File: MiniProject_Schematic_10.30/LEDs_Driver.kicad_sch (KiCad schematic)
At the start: 24 parts, among them U8 IS31FL3254-QFLS4-TR

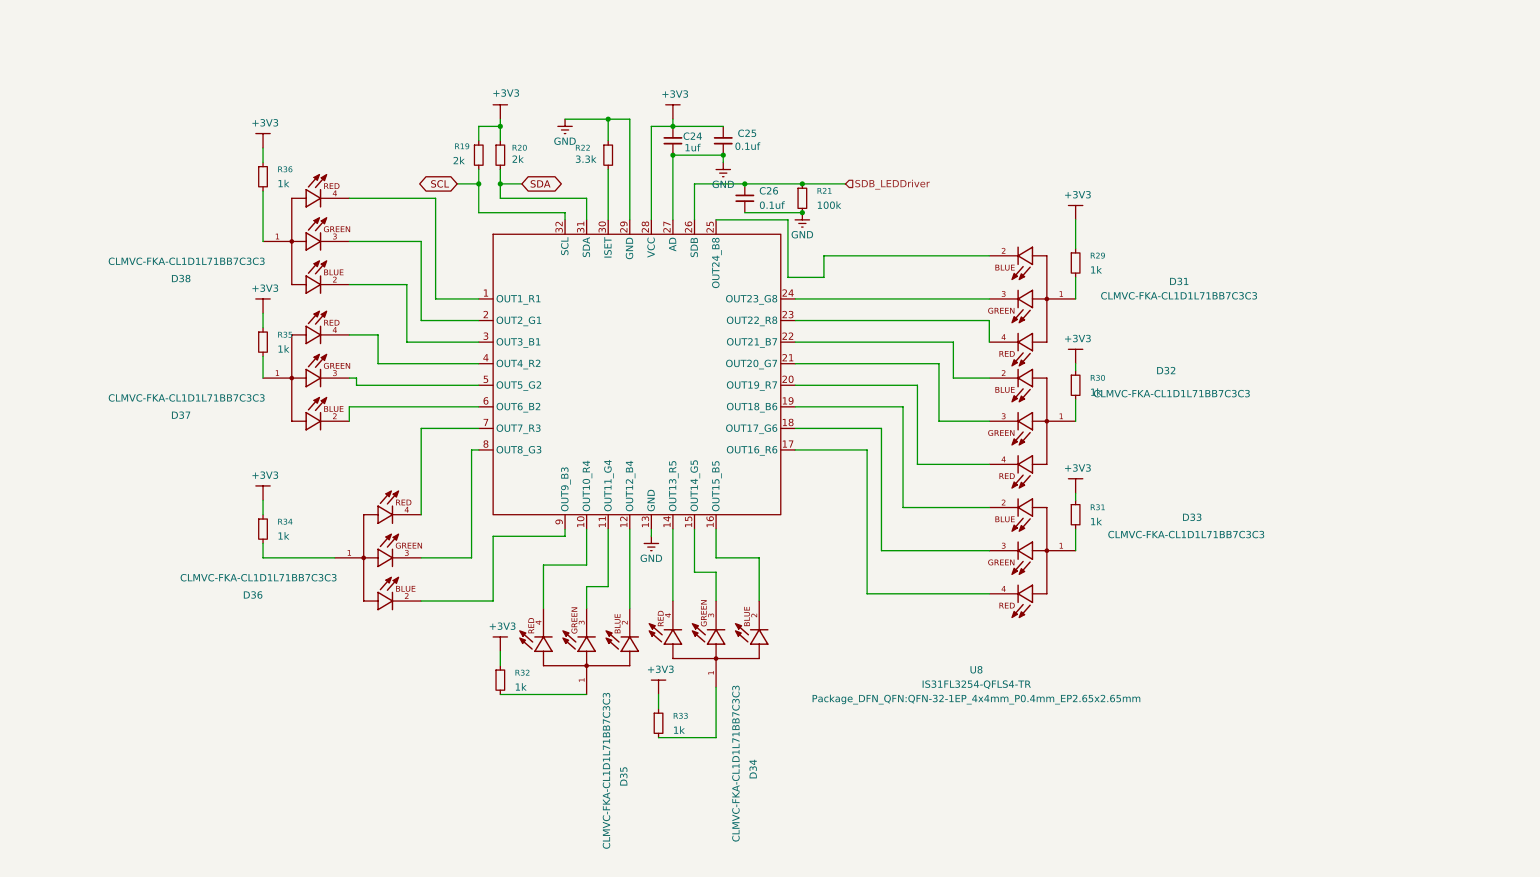
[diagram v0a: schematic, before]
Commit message: Correct the schematic diagram
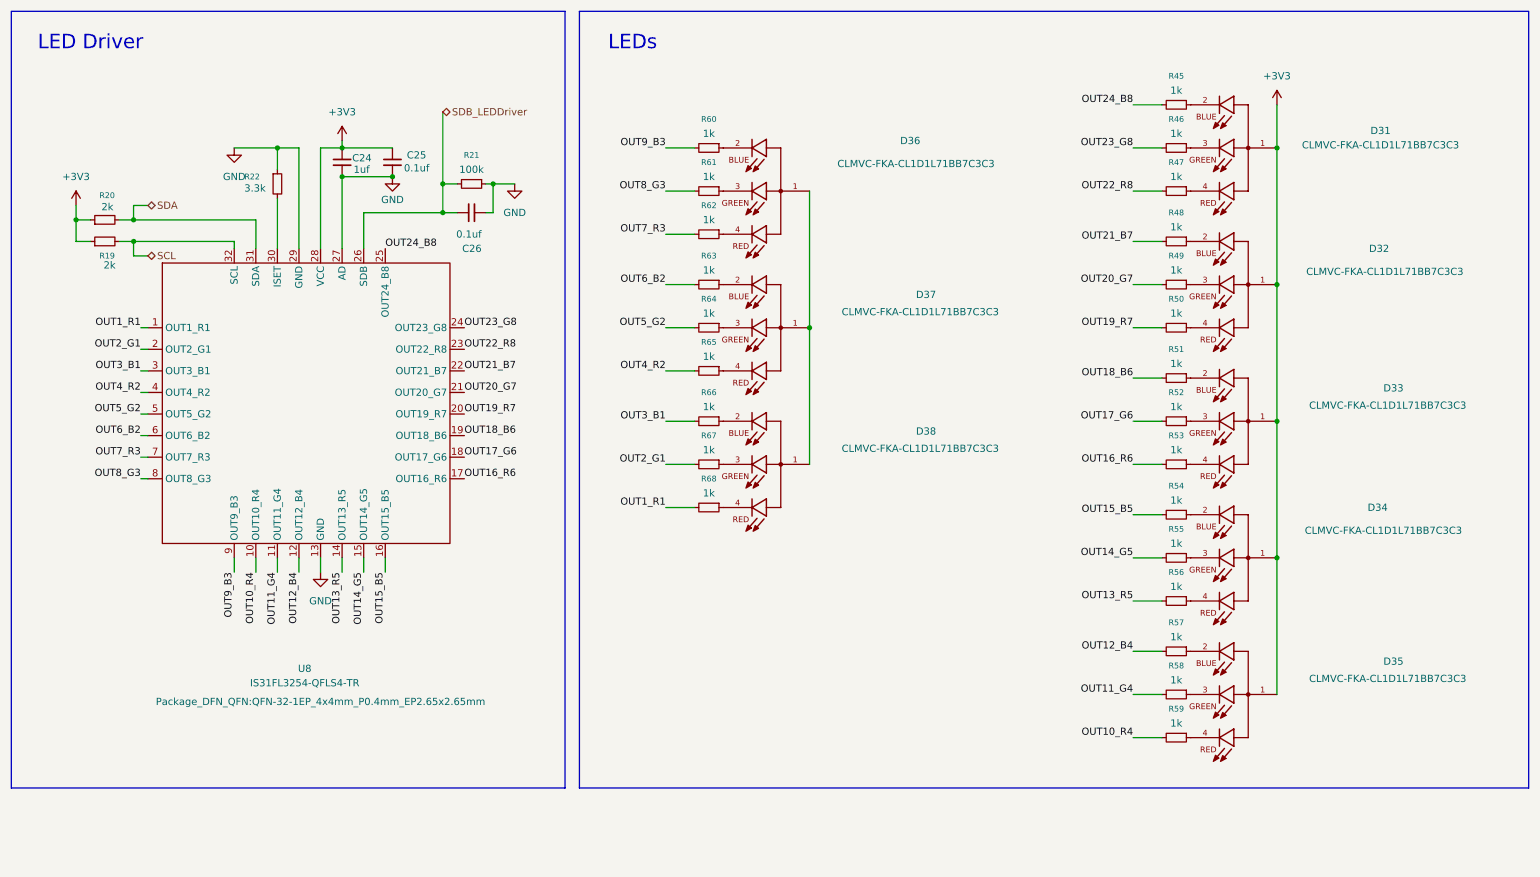
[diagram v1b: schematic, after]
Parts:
- removed R29, R30, R31, R32, R33, R34, R35, R36: 1k, Resistor_SMD:R_0402_1005Metric, symbol Device:R_Small
- added R45, R46, R47, R48, R49, R50, R51, R52, R53, R54, R55, R56, R57, R58, R59, R60, R61, R62, R63, R64, R65, R66, R67, R68: 1k, Resistor_SMD:R_0402_1005Metric, symbol Device:R_Small
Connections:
- net +3V3: now also D31.1, D32.1, D33.1, D34.1, D35.1
- net GND: now also R21.1; no longer R21.2
- net SDB_LEDDriver: now also R21.2; no longer R21.1
- net at D31.2: now also R45.1; no longer U8.25 (OUT24_B8)
- net at D31.3: now also R46.1; no longer U8.24 (OUT23_G8)
- net at D31.4: now also R47.1; no longer U8.23 (OUT22_R8)
- net at D36.1: now also D37.1, D38.1
- net at D36.2: now also R60.1; no longer U8.9 (OUT9_B3)
- net at D36.3: now also R61.1; no longer U8.8 (OUT8_G3)
- net at D36.4: now also R62.1; no longer U8.7 (OUT7_R3)
- net at D37.2: now also R63.1; no longer U8.6 (OUT6_B2)
- net at D37.3: now also R64.1; no longer U8.5 (OUT5_G2)
- net at D37.4: now also R65.1; no longer U8.4 (OUT4_R2)
- net at D38.4: now also R68.1; no longer U8.1 (OUT1_R1)
- net at D35.4: now also R59.1; no longer U8.10 (OUT10_R4)
- net at D35.3: now also R58.1; no longer U8.11 (OUT11_G4)
- net at D35.2: now also R57.1; no longer U8.12 (OUT12_B4)
- net at D34.4: now also R56.1; no longer U8.14 (OUT13_R5)
- net at D34.3: now also R55.1; no longer U8.15 (OUT14_G5)
- net at D34.2: now also R54.1; no longer U8.16 (OUT15_B5)
- net at D33.4: now also R53.1; no longer U8.17 (OUT16_R6)
- net at D33.3: now also R52.1; no longer U8.18 (OUT17_G6)
- net at D33.2: now also R51.1; no longer U8.19 (OUT18_B6)
- net at D38.3: now also R67.1; no longer U8.2 (OUT2_G1)
- net at D32.4: now also R50.1; no longer U8.20 (OUT19_R7)
- net at D32.3: now also R49.1; no longer U8.21 (OUT20_G7)
- net at D32.2: now also R48.1; no longer U8.22 (OUT21_B7)
- net at D38.2: now also R66.1; no longer U8.3 (OUT3_B1)
- new net OUT10_R4: R59.2, U8.10 (OUT10_R4)
- new net OUT11_G4: R58.2, U8.11 (OUT11_G4)
- new net OUT12_B4: R57.2, U8.12 (OUT12_B4)
- new net OUT13_R5: R56.2, U8.14 (OUT13_R5)
- new net OUT14_G5: R55.2, U8.15 (OUT14_G5)
- new net OUT15_B5: R54.2, U8.16 (OUT15_B5)
- new net OUT16_R6: R53.2, U8.17 (OUT16_R6)
- new net OUT17_G6: R52.2, U8.18 (OUT17_G6)
- new net OUT18_B6: R51.2, U8.19 (OUT18_B6)
- new net OUT19_R7: R50.2, U8.20 (OUT19_R7)
- new net OUT1_R1: R68.2, U8.1 (OUT1_R1)
- new net OUT20_G7: R49.2, U8.21 (OUT20_G7)
- new net OUT21_B7: R48.2, U8.22 (OUT21_B7)
- new net OUT22_R8: R47.2, U8.23 (OUT22_R8)
- new net OUT23_G8: R46.2, U8.24 (OUT23_G8)
- new net OUT24_B8: R45.2, U8.25 (OUT24_B8)
- new net OUT2_G1: R67.2, U8.2 (OUT2_G1)
- new net OUT3_B1: R66.2, U8.3 (OUT3_B1)
- new net OUT4_R2: R65.2, U8.4 (OUT4_R2)
- new net OUT5_G2: R64.2, U8.5 (OUT5_G2)
- new net OUT6_B2: R63.2, U8.6 (OUT6_B2)
- new net OUT7_R3: R62.2, U8.7 (OUT7_R3)
- new net OUT8_G3: R61.2, U8.8 (OUT8_G3)
- new net OUT9_B3: R60.2, U8.9 (OUT9_B3)
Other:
- note added: "LED Driver"
- note added: "LEDs"
- moved on the sheet: C24, C25, C26, R19, R20, R22, U8
